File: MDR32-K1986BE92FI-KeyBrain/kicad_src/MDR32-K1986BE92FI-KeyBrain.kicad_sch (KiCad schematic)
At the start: 25 parts, among them J1 Conn_01x12, J2 Conn_01x12, J3 USB_C_Receptacle_USB2.0_16P, J4 Conn_01x04, U1 USBLC6-2SC6, U2 AP2112K-3.3

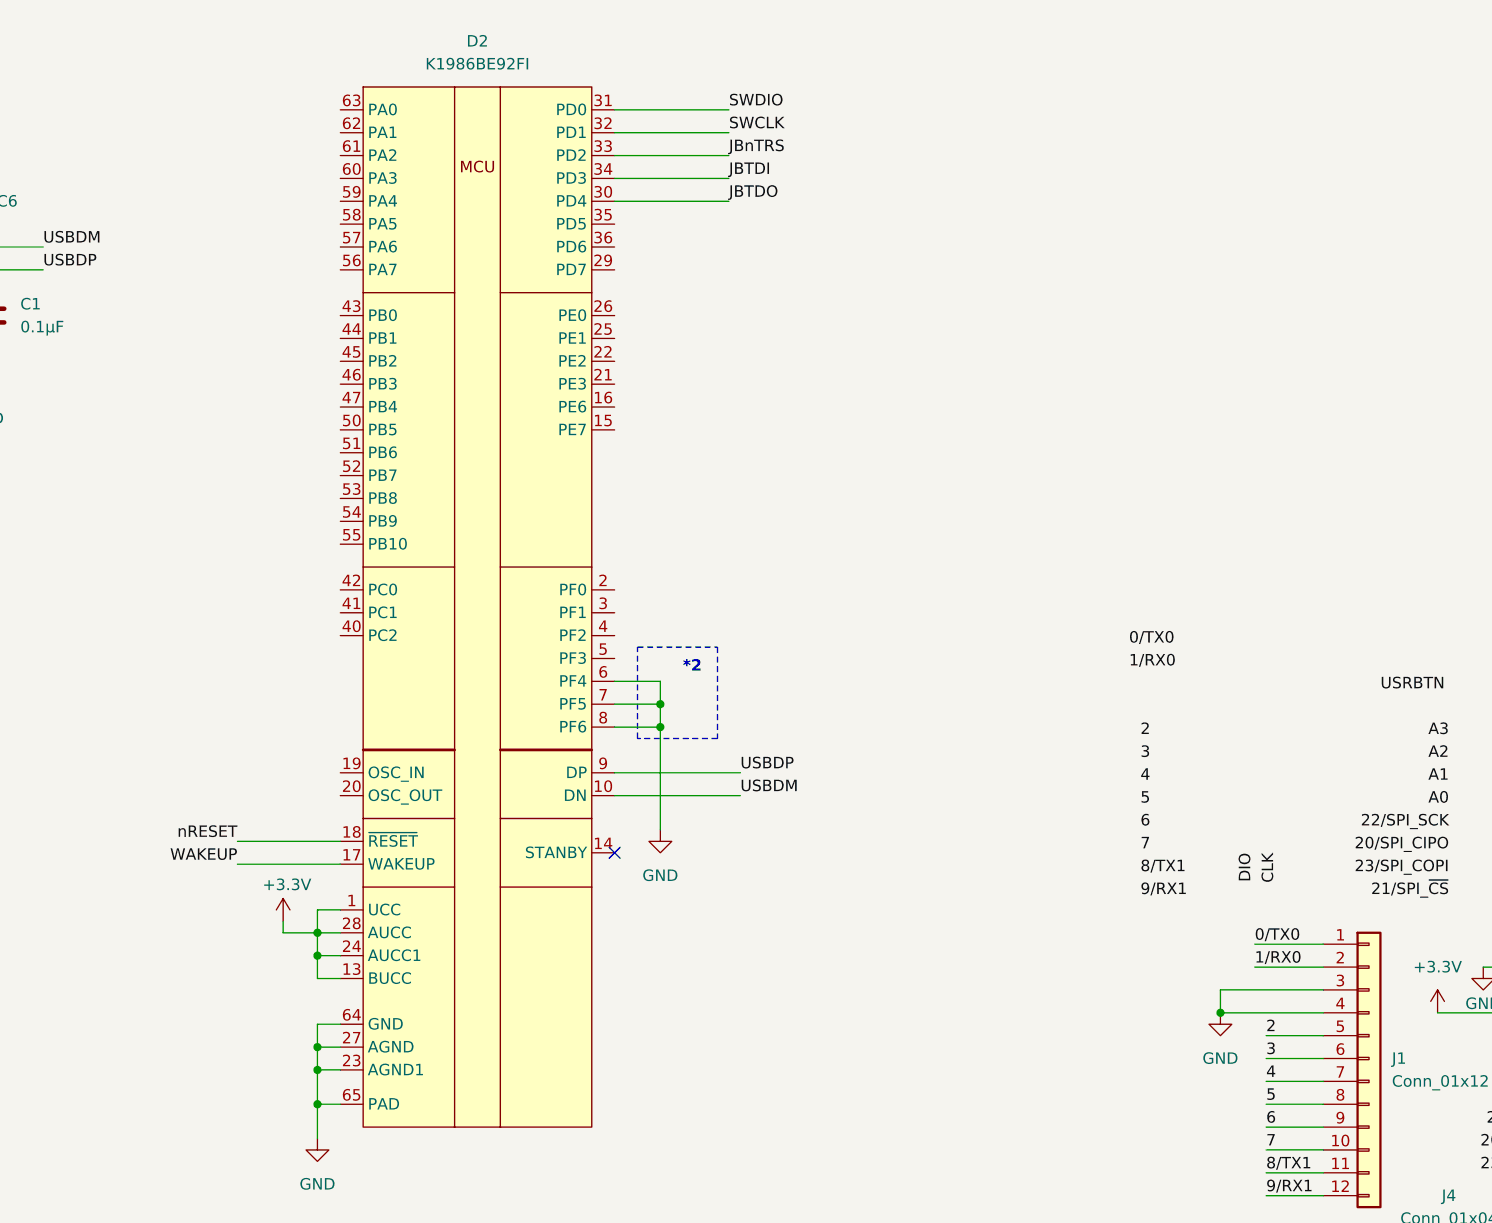
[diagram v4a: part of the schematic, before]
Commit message: MDR32-K1986BE92FI-KeyBrain: некоторые пины
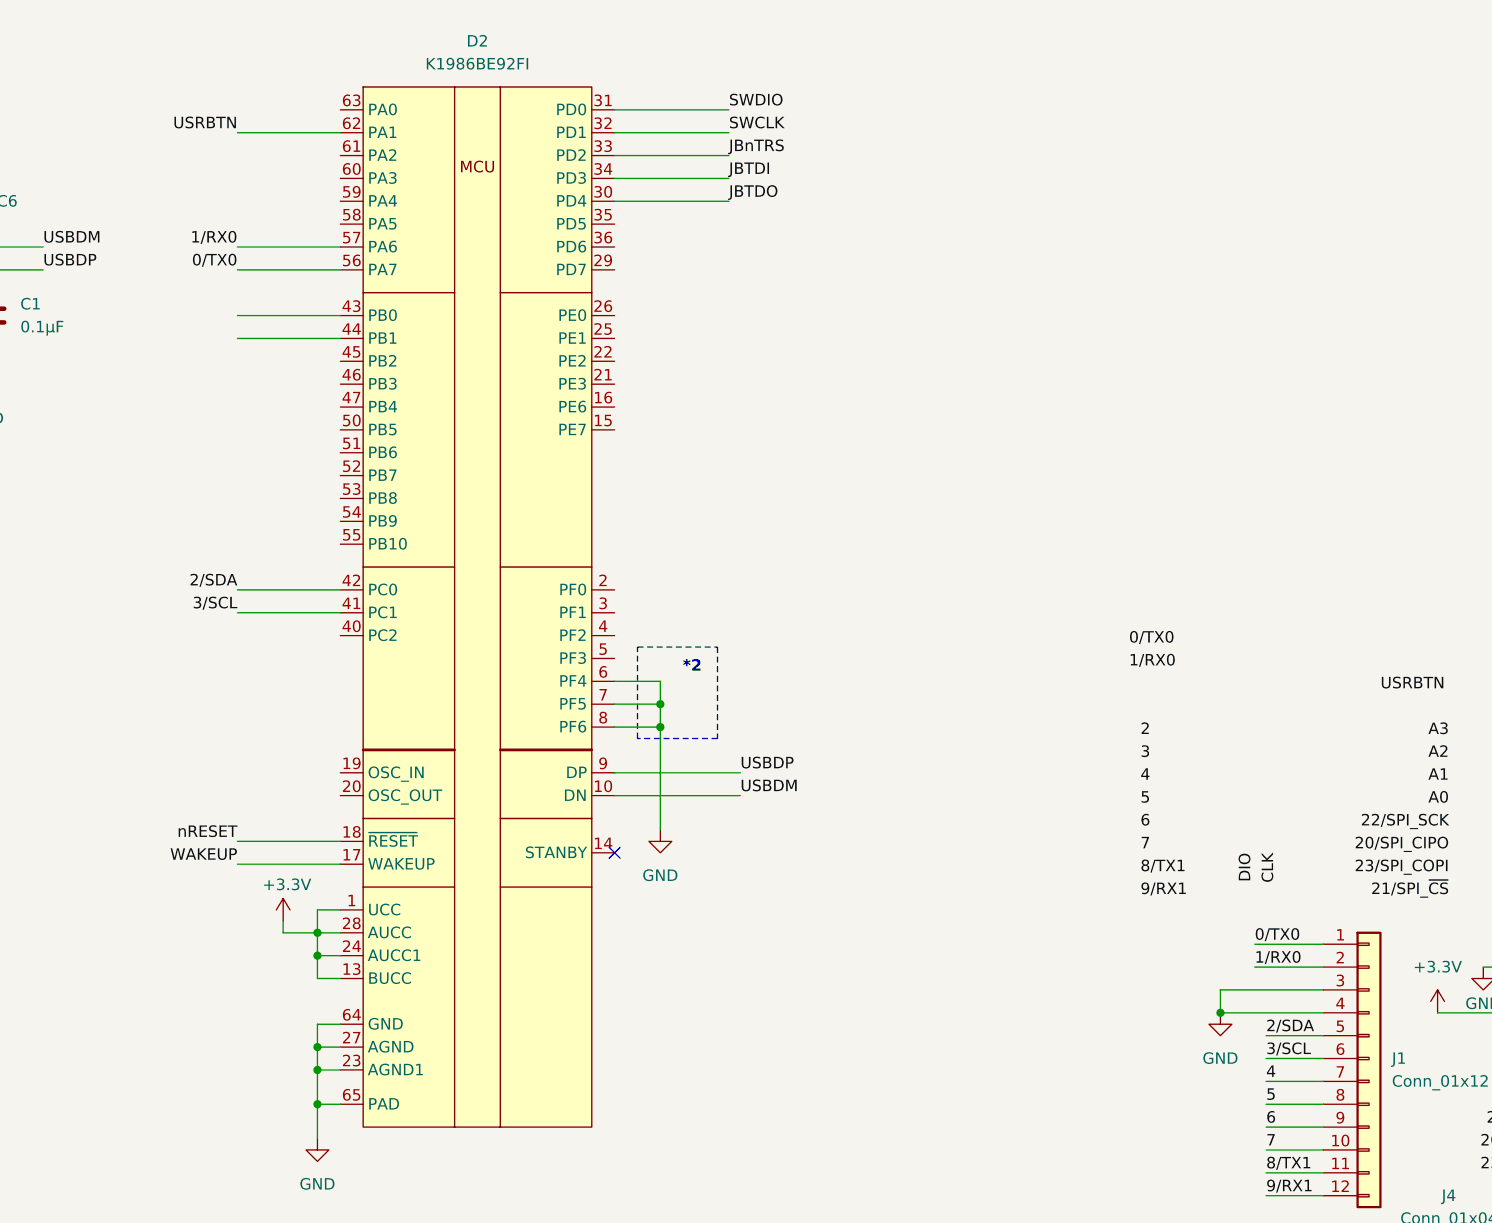
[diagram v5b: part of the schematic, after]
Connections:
- net 0/TX0: no longer J1.1 (Pin_1)
- net 2: no longer J1.5 (Pin_5)
- net 3: no longer J1.6 (Pin_6)
- net USRBTN: now also D2.62 (PA1)
- net 3/SCL: now reaches D2.41 (PC1)
- net 3/SCL: now also J1.6 (Pin_6)
- net 2/SDA: now reaches D2.42 (PC0)
- net 2/SDA: now also J1.5 (Pin_5)
- net 0/TX0: now reaches D2.56 (PA7)
- net 0/TX0: now also J1.1 (Pin_1)
- net 1/RX0: now reaches D2.57 (PA6)
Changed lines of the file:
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@@
 	(wire
 		(pts
+			(xy 113.03 52.07) (xy 124.46 52.07)
+		)
+		(stroke
+			(width 0)
+			(type default)
+		)
+	)
+	(wire
+		(pts
 			(xy 53.34 171.45) (xy 53.34 173.99)
 		)
@@
 	(wire
 		(pts
+			(xy 113.03 82.55) (xy 124.46 82.55)
+		)
+		(stroke
+			(width 0)
+			(type default)
+		)
+	)
+	(wire
+		(pts
 			(xy 97.79 181.61) (xy 97.79 182.88)
 		)
@@
 	(wire
 		(pts
+			(xy 113.03 80.01) (xy 124.46 80.01)
+		)
+		(stroke
+			(width 0)
+			(type default)
+		)
+	)
+	(wire
+		(pts
 			(xy 121.92 118.11) (xy 121.92 115.57)
 		)
@@
 	(wire
 		(pts
+			(xy 113.03 44.45) (xy 124.46 44.45)
+		)
+		(stroke
+			(width 0)
+			(type default)
+		)
+	)
+	(wire
+		(pts
 			(xy 154.94 100.33) (xy 168.91 100.33)
 		)
@@
 	(wire
 		(pts
+			(xy 113.03 41.91) (xy 124.46 41.91)
+		)
+		(stroke
+			(width 0)
+			(type default)
+		)
+	)
+	(wire
+		(pts
 			(xy 80.01 41.91) (xy 91.44 41.91)
 		)
@@
 	(wire
 		(pts
+			(xy 113.03 49.53) (xy 124.46 49.53)
+		)
+		(stroke
+			(width 0)
+			(type default)
+		)
+	)
+	(wire
+		(pts
 			(xy 154.94 34.29) (xy 167.64 34.29)
 		)
@@
 	(wire
 		(pts
+			(xy 113.03 29.21) (xy 124.46 29.21)
+		)
+		(stroke
+			(width 0)
+			(type default)
+		)
+	)
+	(wire
+		(pts
 			(xy 46.99 41.91) (xy 69.85 41.91)
 		)
@@
 		)
 	)
+	(label "USRBTN"
+		(at 113.03 29.21 180)
+		(effects
+			(font
+				(size 1.27 1.27)
+			)
+			(justify right bottom)
+		)
+	)
 	(label "JBnTRS"
 		(at 57.15 95.25 180)
@@
 		)
 	)
+	(label "0{slash}TX0"
+		(at 113.03 44.45 180)
+		(effects
+			(font
+				(size 1.27 1.27)
+			)
+			(justify right bottom)
+		)
+	)
 	(label "5"
 		(at 213.36 104.14 0)
@@
 		)
 	)
+	(label "1{slash}RX0"
+		(at 113.03 41.91 180)
+		(effects
+			(font
+				(size 1.27 1.27)
+			)
+			(justify right bottom)
+		)
+	)
 	(label "1/RX0"
 		(at 212.09 88.9 0)
@@
 		)
 	)
-	(label "3"
+	(label "3{slash}SCL"
 		(at 227.33 132.08 0)
 		(effects
@@
 		)
 	)
-	(label "0/TX0"
+	(label "0{slash}TX0"
 		(at 226.06 119.38 0)
 		(effects
@@
 		)
 	)
+	(label "2{slash}SDA"
+		(at 113.03 80.01 180)
+		(effects
+			(font
+				(size 1.27 1.27)
+			)
+			(justify right bottom)
+		)
+	)
 	(label "USBDP"
 		(at 91.44 44.45 0)
@@
 		)
 	)
+	(label "3{slash}SCL"
+		(at 113.03 82.55 180)
+		(effects
+			(font
+				(size 1.27 1.27)
+			)
+			(justify right bottom)
+		)
+	)
 	(label "USBDM"
 		(at 168.91 102.87 0)
@@
 		)
 	)
-	(label "2"
+	(label "2{slash}SDA"
 		(at 227.33 129.54 0)
 		(effects

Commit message: MDR32-K1986BE92FI-KeyBrain: Пробуем вариант с портам A
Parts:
- added JP1: EnJTAG_A, symbol Jumper:Jumper_2_Bridged
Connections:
- net +3.3V: now also JP1.2 (B)
- net A0: now also D2.33 (PD2)
- net A1: now also D2.34 (PD3)
- net A2: now also D2.30 (PD4)
- net A3: now also D2.35 (PD5)
- net GND: no longer D2.6 (PF4)
- net SWCLK: now also D2.45 (PB2); no longer D2.32 (PD1)
- net SWDIO: now also D2.44 (PB1); no longer D2.31 (PD0)
- net 23/SPI_COPI: now reaches D2.2 (PF0)
- net 22/SPI_SCK: now reaches D2.3 (PF1)
- net 21/SPI_~{CS}: now reaches D2.4 (PF2)
- net JATDO: now reaches D2.43 (PB0)
- net JATDO: now also R7.1
- net JATDI: now reaches D2.46 (PB3)
- net JATDI: now also R6.1
- net JAnTRS: now reaches D2.47 (PB4)
- net JAnTRS: now also R5.1
- net 20/SPI_CIPO: now reaches D2.5 (PF3)
- removed net JBTDI: D2.34 (PD3), R6.1
- removed net JBTDO: D2.30 (PD4), R7.1
- removed net JBnTRS: D2.33 (PD2), R5.1
- new net 8/TX1: D2.32 (PD1)
- new net 9/RX1: D2.31 (PD0)
- new net JTAG_MODE: D2.6 (PF4), JP1.1 (A)
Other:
- note added: "*1 Шунтирующие конденсаторы, обязательно около VCC, AVCC и AVCC1 *2 Активен режим JTAG_A, режим JTAG_B доступен только с манипуляцией *3 Опционально, но желательно *? возможно лучше JTAG_B заменить на JTAG_A чтобы аналоговый порт был доступен целиком в таком случае, в случае глюков МК, не возможно будет его восстановить"
- note removed: "*1 Шунтирующие конденсаторы, обязательно около VCC, AVCC и AVCC1 *2 Доступен только режим JTAG_B *3 Опционально, но желательно *? возможно лучше JTAG_B заменить на JTAG_A чтобы аналоговый порт был доступен целиком в таком случае, в случае глюков МК, не возможно будет его восстановить"
- moved on the sheet: R3, R4, R5, R6, R7, R8, R9

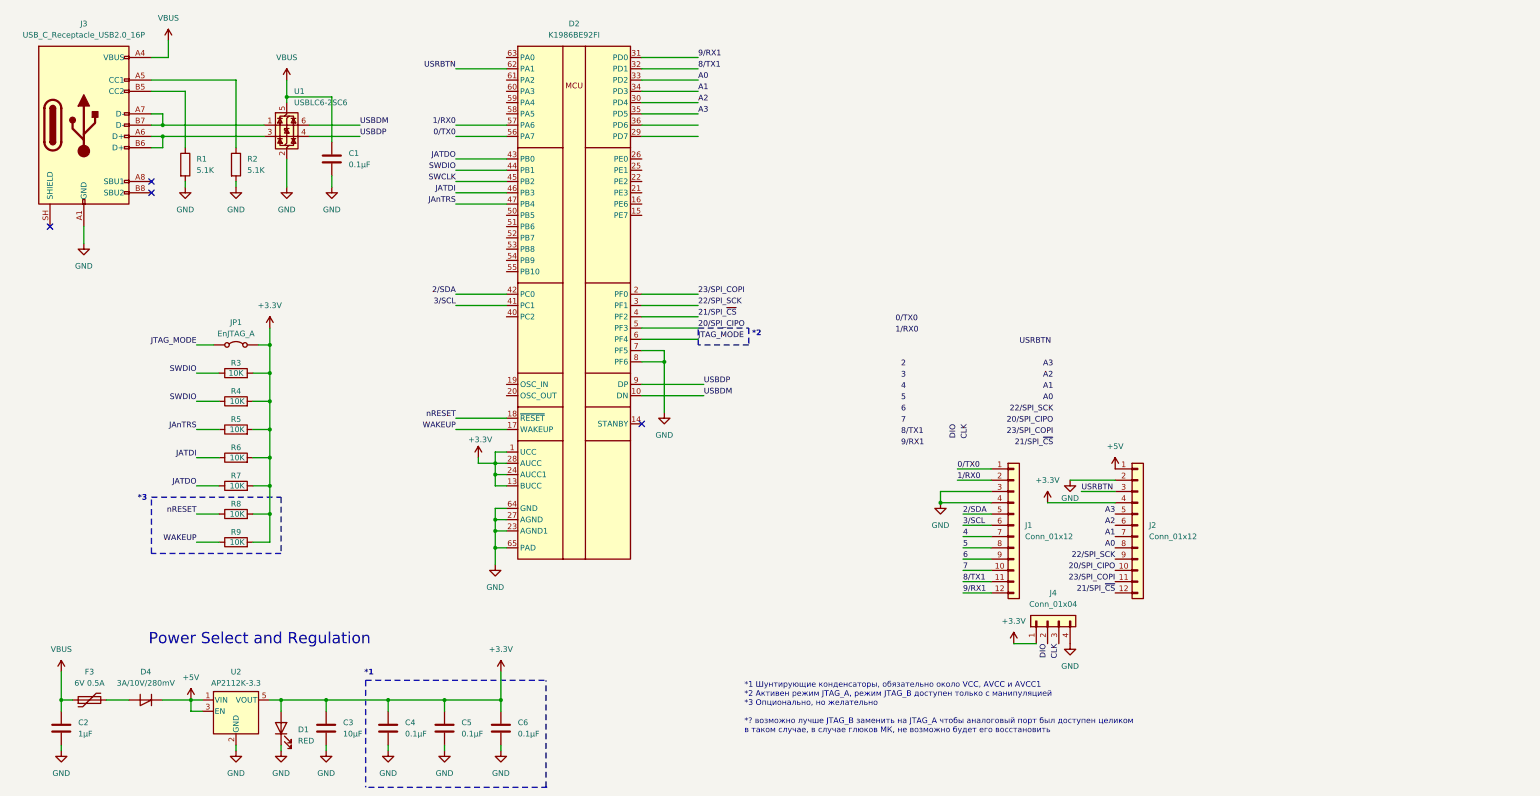
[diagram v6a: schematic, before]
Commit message: MDR32-K1986BE92FI-KeyBrain: add diff pairs and comments on schematic
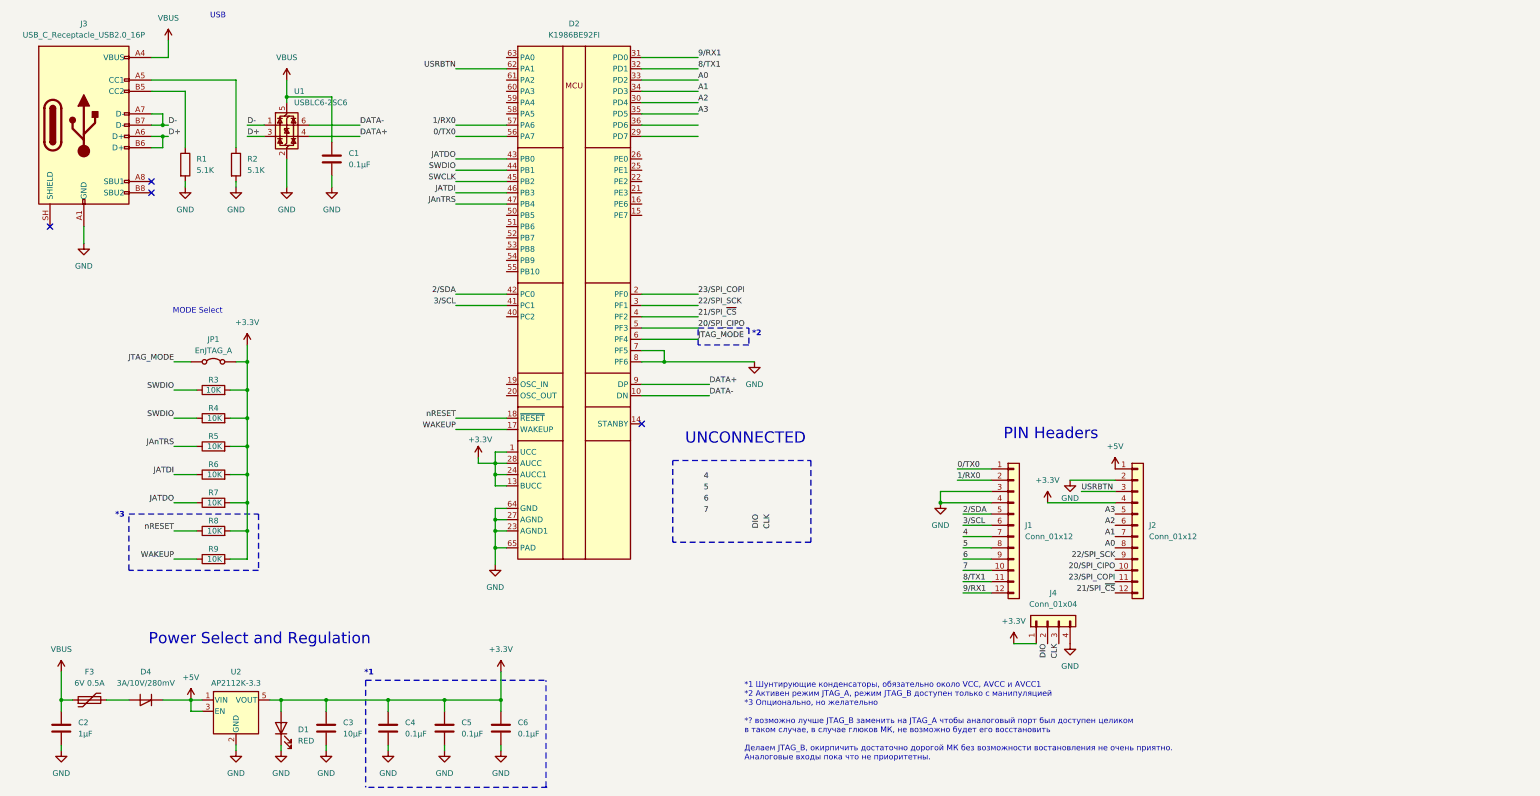
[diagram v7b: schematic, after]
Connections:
- net D-: now reaches J3.A7 (D-), J3.B7 (D-), U1.1 (I/O1)
- net D+: now reaches J3.A6 (D+), J3.B6 (D+), U1.3 (I/O2)
- net USBDM renamed DATA-
- net USBDP renamed DATA+
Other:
- note added: "*1 Шунтирующие конденсаторы, обязательно около VCC, AVCC и AVCC1 *2 Активен режим JTAG_A, режим JTAG_B доступен только с манипуляцией *3 Опционально, но желательно *? возможно лучше JTAG_B заменить на JTAG_A чтобы аналоговый порт был доступен целиком в таком случае, в случае глюков МК, не возможно будет его восстановить Делаем JTAG_B, окирпичить достаточно дорогой МК без возможности востановления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"
- note added: "MODE Select"
- note added: "PIN Headers"
- note added: "UNCONNECTED"
- note added: "USB"
- note removed: "*1 Шунтирующие конденсаторы, обязательно около VCC, AVCC и AVCC1 *2 Активен режим JTAG_A, режим JTAG_B доступен только с манипуляцией *3 Опционально, но желательно *? возможно лучше JTAG_B заменить на JTAG_A чтобы аналоговый порт был доступен целиком в таком случае, в случае глюков МК, не возможно будет его восстановить"
- moved on the sheet: JP1, R3, R4, R5, R6, R7, R8, R9

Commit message: MDR32-K1986BE92FI-KeyBrain: add footprints and crystal
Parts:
- added C12, C7: 10pF, MDR32-K1986BE92FI-DK:C_0603_1608Metric, symbol MDR32-K1986BE92FI-DK:C
- added D2: GREEN, LED_SMD:LED_0603_1608Metric_Pad1.05x0.95mm_HandSolder, symbol Device:LED
- added Y1: 8MHz, Crystal:Crystal_SMD_3225-4Pin_3.2x2.5mm_HandSoldering, symbol MDR32-K1986BE92FI-DK:Crystal_GND24
- C1, C2, C3, C4, C5, C6: footprint (none) -> Capacitor_SMD:C_0603_1608Metric_Pad1.08x0.95mm_HandSolder
- D1: footprint (none) -> LED_SMD:LED_0603_1608Metric_Pad1.05x0.95mm_HandSolder
- D4: footprint (none) -> Diode_SMD:D_0603_1608Metric_Pad1.05x0.95mm_HandSolder
- R1, R2, R3, R4, R5, R6, R7, R8, R9: footprint (none) -> Resistor_SMD:R_0603_1608Metric_Pad0.98x0.95mm_HandSolder
- renumbered U2 to U1, D2 to U2, U1 to U3
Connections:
- net GND: now also C12.2, C7.2, D2.1 (K), Y1.2, Y1.4
- net OSC_IN: now reaches U2.19 (OSC_IN)
- net OSC_IN: now also C7.1, Y1.1
- net OSC_OUT: now reaches U2.20 (OSC_OUT)
- net OSC_OUT: now also C12.1, Y1.3
- new net USRLED: D2.2 (A)
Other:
- note added: "Crystal"
- moved on the sheet: JP1, R3, R4, R5, R6, R7, R8, R9
